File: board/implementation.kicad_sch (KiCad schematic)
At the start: 0 parts

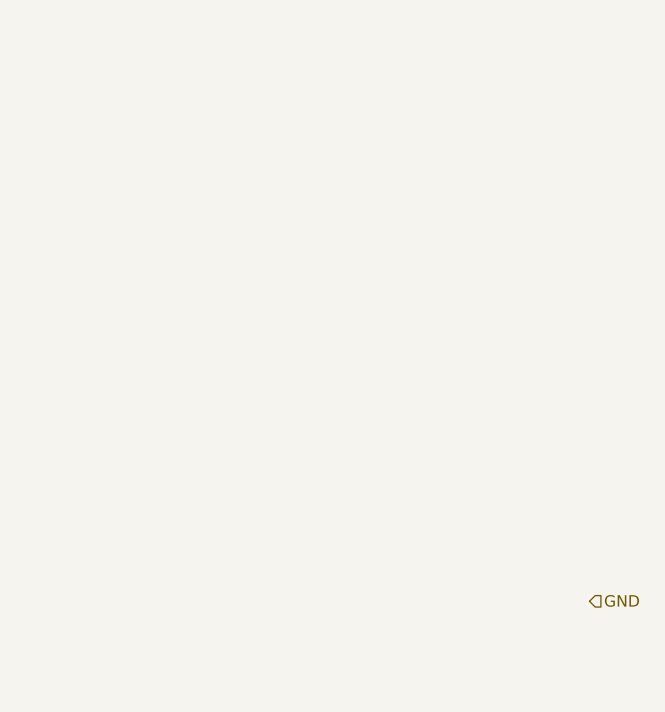
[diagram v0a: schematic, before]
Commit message: Add footprint, schema, 3D Model | Start circuit design
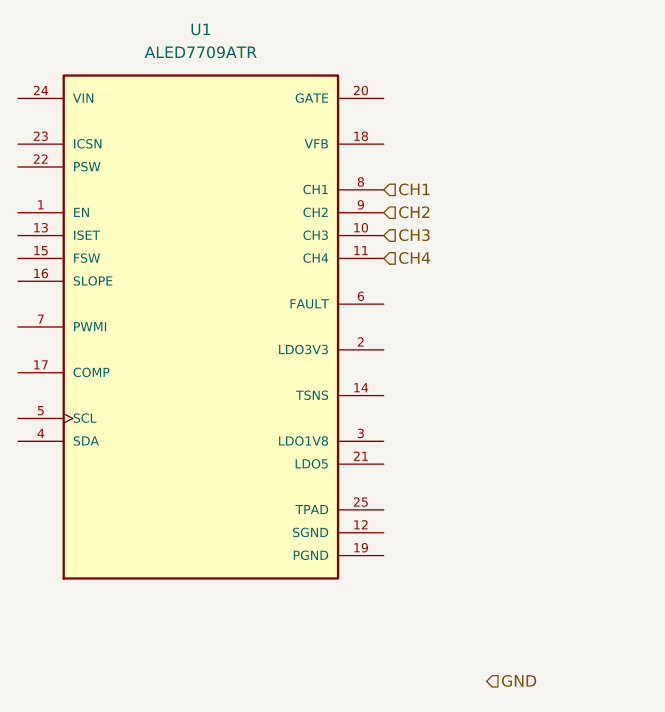
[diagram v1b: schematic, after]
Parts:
- added U1: ALED7709ATR, QFN65P500X500X90-25N, symbol ALED7709ATR:ALED7709ATR
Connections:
- new net CH1: U1.8 (CH1)
- new net CH2: U1.9 (CH2)
- new net CH3: U1.10 (CH3)
- new net CH4: U1.11 (CH4)
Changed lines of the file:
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@@
 (kicad_sch (version 20211123) (generator eeschema)
   (paper "A4")
-  (hierarchical_label "GND" (shape input) (at 194.31 120.65 0)
+  (hierarchical_label "CH1" (shape input) (at 171.45 74.93 0)
     (effects (font (size 1.27 1.27)) (justify left))
   )
+  (hierarchical_label "CH4" (shape input) (at 171.45 82.55 0)
+    (effects (font (size 1.27 1.27)) (justify left))
+  )
+  (hierarchical_label "GND" (shape input) (at 182.88 129.54 0)
+    (effects (font (size 1.27 1.27)) (justify left))
+  )
+  (hierarchical_label "CH3" (shape input) (at 171.45 80.01 0)
+    (effects (font (size 1.27 1.27)) (justify left))
+  )
+  (hierarchical_label "CH2" (shape input) (at 171.45 77.47 0)
+    (effects (font (size 1.27 1.27)) (justify left))
+  )
+  (symbol (lib_id "ALED7709ATR:ALED7709ATR") (at 151.13 90.17 0) (unit 1)
+    (in_bom yes) (on_board yes) (fields_autoplaced)
+    (property "Reference" "U1" (id 0) (at 151.13 57.15 0))
+    (property "Value" "ALED7709ATR" (id 1) (at 151.13 59.69 0))
+    (property "Footprint" "QFN65P500X500X90-25N" (id 2) (at 151.13 90.17 0)
+      (effects (font (size 1.27 1.27)) (justify bottom) hide)
+    )
+    (property "Datasheet" "https://www.st.com/resource/en/datasheet/aled7709.pdf" (id 3) (at 151.13 90.17 0)
+      (effects (font (size 1.27 1.27)) hide)
+    )
+    (property "SNAPEDA_PACKAGE_ID" "" (id 4) (at 151.13 90.17 0)
+      (effects (font (size 1.27 1.27)) (justify bottom) hide)
+    )
+    (property "B_NOM" "0.3" (id 5) (at 151.13 90.17 0)
+      (effects (font (size 1.27 1.27)) (justify bottom) hide)
+    )
+    (property "EMAX" "" (id 6) (at 151.13 90.17 0)
+      (effects (font (size 1.27 1.27)) (justify bottom) hide)
+    )
+    (property "D_MAX" "5.1" (id 7) (at 151.13 90.17 0)
+      (effects (font (size 1.27 1.27)) (justify bottom) hide)
+    )
+    (property "BALL_COLUMNS" "" (id 8) (at 151.13 90.17 0)
+      (effects (font (size 1.27 1.27)) (justify bottom) hide)
+    )
+    (property "PIN_COUNT_D" "6.0" (id 9) (at 151.13 90.17 0)
+      (effects (font (size 1.27 1.27)) (justify bottom) hide)
+    )
+    (property "THERMAL_PAD" "" (id 10) (at 151.13 90.17 0)
+      (effects (font (size 1.27 1.27)) (justify bottom) hide)
+    )
+    (property "DMAX" "" (id 11) (at 151.13 90.17 0)
+      (effects (font (size 1.27 1.27)) (justify bottom) hide)
+    )
+    (property "B_MAX" "0.35" (id 12) (at 151.13 90.17 0)
+      (effects (font (size 1.27 1.27)) (justify bottom) hide)
+    )
+    (property "EMIN" "" (id 13) (at 151.13 90.17 0)
+      (effects (font (size 1.27 1.27)) (justify bottom) hide)
+    )
+    (property "JEDEC" "" (id 14) (at 151.13 90.17 0)
+      (effects (font (size 1.27 1.27)) (justify bottom) hide)
+    )
+    (property "ENOM" "0.65" (id 15) (at 151.13 90.17 0)
+      (effects (font (size 1.27 1.27)) (justify bottom) hide)
+    )
+    (property "D_NOM" "5.0" (id 16) (at 151.13 90.17 0)
+      (effects (font (size 1.27 1.27)) (justify bottom) hide)
+    )
+    (property "VACANCIES" "" (id 17) (at 151.13 90.17 0)
+      (effects (font (size 1.27 1.27)) (justify bottom) hide)
+    )
+    (property "L_MAX" "0.5" (id 18) (at 151.13 90.17 0)
+      (effects (font (size 1.27 1.27)) (justify bottom) hide)
+    )
+    (property "A_MAX" "0.9" (id 19) (at 151.13 90.17 0)
+      (effects (font (size 1.27 1.27)) (justify bottom) hide)
+    )
+    (property "E2_NOM" "3.5" (id 20) (at 151.13 90.17 0)
+      (effects (font (size 1.27 1.27)) (justify bottom) hide)
+    )
+    (property "D2_NOM" "3.5" (id 21) (at 151.13 90.17 0)
+      (effects (font (size 1.27 1.27)) (justify bottom) hide)
+    )
+    (property "PARTREV" "1" (id 22) (at 151.13 90.17 0)
+      (effects (font (size 1.27 1.27)) (justify bottom) hide)
+    )
+    (property "DNOM" "" (id 23) (at 151.13 90.17 0)
+      (effects (font (size 1.27 1.27)) (justify bottom) hide)
+    )
+    (property "DMIN" "" (id 24) (at 151.13 90.17 0)
+      (effects (font (size 1.27 1.27)) (justify bottom) hide)
+    )
+    (property "E_NOM" "5.0" (id 25) (at 151.13 90.17 0)
+      (effects (font (size 1.27 1.27)) (justify bottom) hide)
+    )
+    (property "BALL_ROWS" "" (id 26) (at 151.13 90.17 0)
+      (effects (font (size 1.27 1.27)) (justify bottom) hide)
+    )
+    (property "B_MIN" "0.25" (id 27) (at 151.13 90.17 0)
+      (effects (font (size 1.27 1.27)) (justify bottom) hide)
+    )
+    (property "STANDARD" "IPC 7351B" (id 28) (at 151.13 90.17 0)
+      (effects (font (size 1.27 1.27)) (justify bottom) hide)
+    )
+    (property "L_NOM" "0.4" (id 29) (at 151.13 90.17 0)
+      (effects (font (size 1.27 1.27)) (justify bottom) hide)
+    )
+    (property "MANUFACTURER" "STMicroelectronics" (id 30) (at 151.13 90.17 0)
+      (effects (font (size 1.27 1.27)) (justify bottom) hide)
+    )
+    (property "IPC" "" (id 31) (at 151.13 90.17 0)
+      (effects (font (size 1.27 1.27)) (justify bottom) hide)
+    )
+    (property "PIN_COLUMNS" "" (id 32) (at 151.13 90.17 0)
+      (effects (font (size 1.27 1.27)) (justify bottom) hide)
+    )
+    (property "PIN_COUNT_E" "6.0" (id 33) (at 151.13 90.17 0)
+      (effects (font (size 1.27 1.27)) (justify bottom) hide)
+    )
+    (property "BODY_DIAMETER" "" (id 34) (at 151.13 90.17 0)
+      (effects (font (size 1.27 1.27)) (justify bottom) hide)
+    )
+    (property "E_MIN" "4.9" (id 35) (at 151.13 90.17 0)
+      (effects (font (size 1.27 1.27)) (justify bottom) hide)
+    )
+    (property "PACKAGE_TYPE" "" (id 36) (at 151.13 90.17 0)
+      (effects (font (size 1.27 1.27)) (justify bottom) hide)
+    )
+    (property "D_MIN" "4.9" (id 37) (at 151.13 90.17 0)
+      (effects (font (size 1.27 1.27)) (justify bottom) hide)
+    )
+    (property "PINS" "" (id 38) (at 151.13 90.17 0)
+      (effects (font (size 1.27 1.27)) (justify bottom) hide)
+    )
+    (property "L_MIN" "0.3" (id 39) (at 151.13 90.17 0)
+      (effects (font (size 1.27 1.27)) (justify bottom) hide)
+    )
+    (property "E_MAX" "5.1" (id 40) (at 151.13 90.17 0)
+      (effects (font (size 1.27 1.27)) (justify bottom) hide)
+    )
+    (pin "1")
+    (pin "10")
+    (pin "11")
+    (pin "12")
+    (pin "13")
+    (pin "14")
+    (pin "15")
+    (pin "16")
+    (pin "17")
+    (pin "18")
+    (pin "19")
+    (pin "2")
+    (pin "20")
+    (pin "21")
+    (pin "22")
+    (pin "23")
+    (pin "24")
+    (pin "25")
+    (pin "3")
+    (pin "4")
+    (pin "5")
+    (pin "6")
+    (pin "7")
+    (pin "8")
+    (pin "9")
+  )
 )

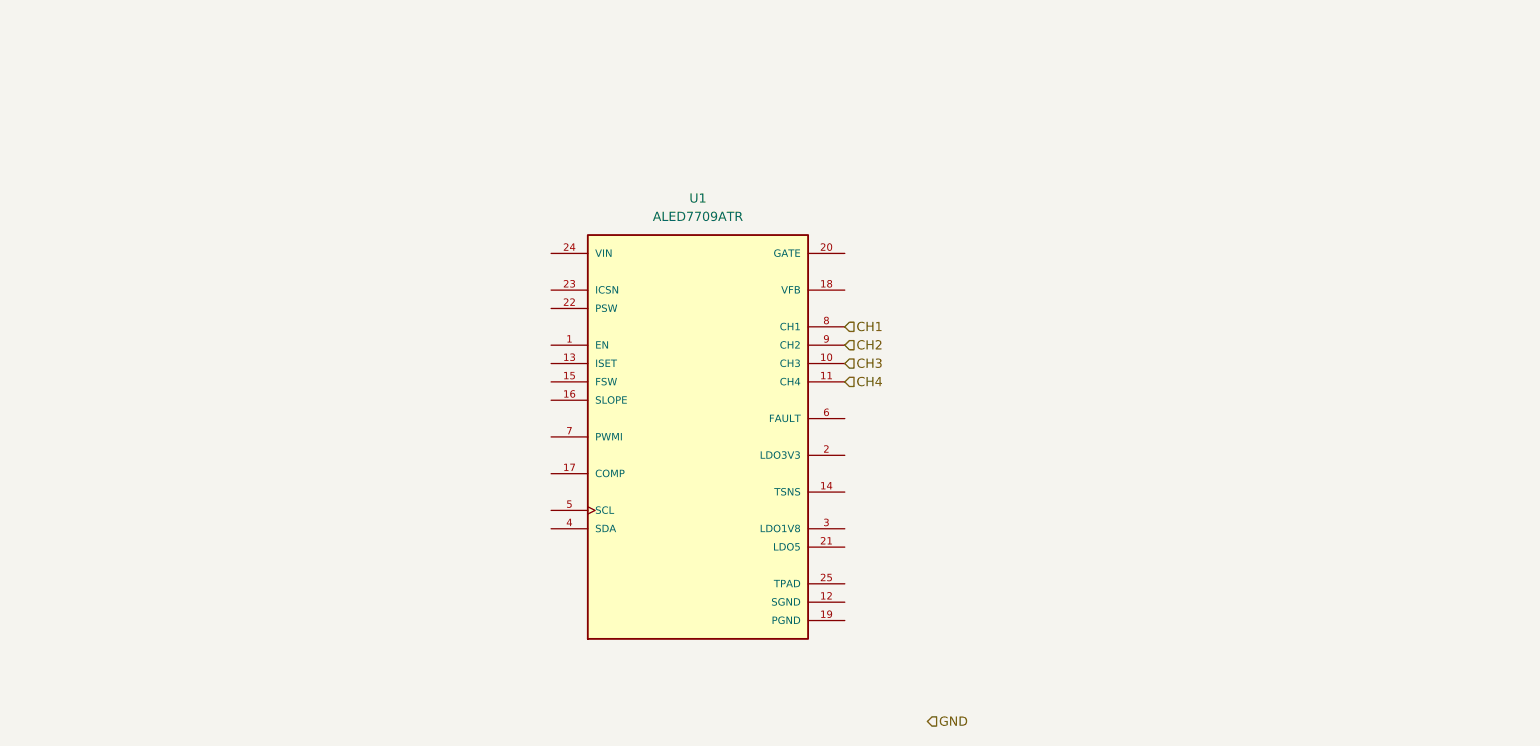
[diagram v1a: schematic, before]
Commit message: Add footprint, symbol and 3D modell | Add parts for reference cicuit
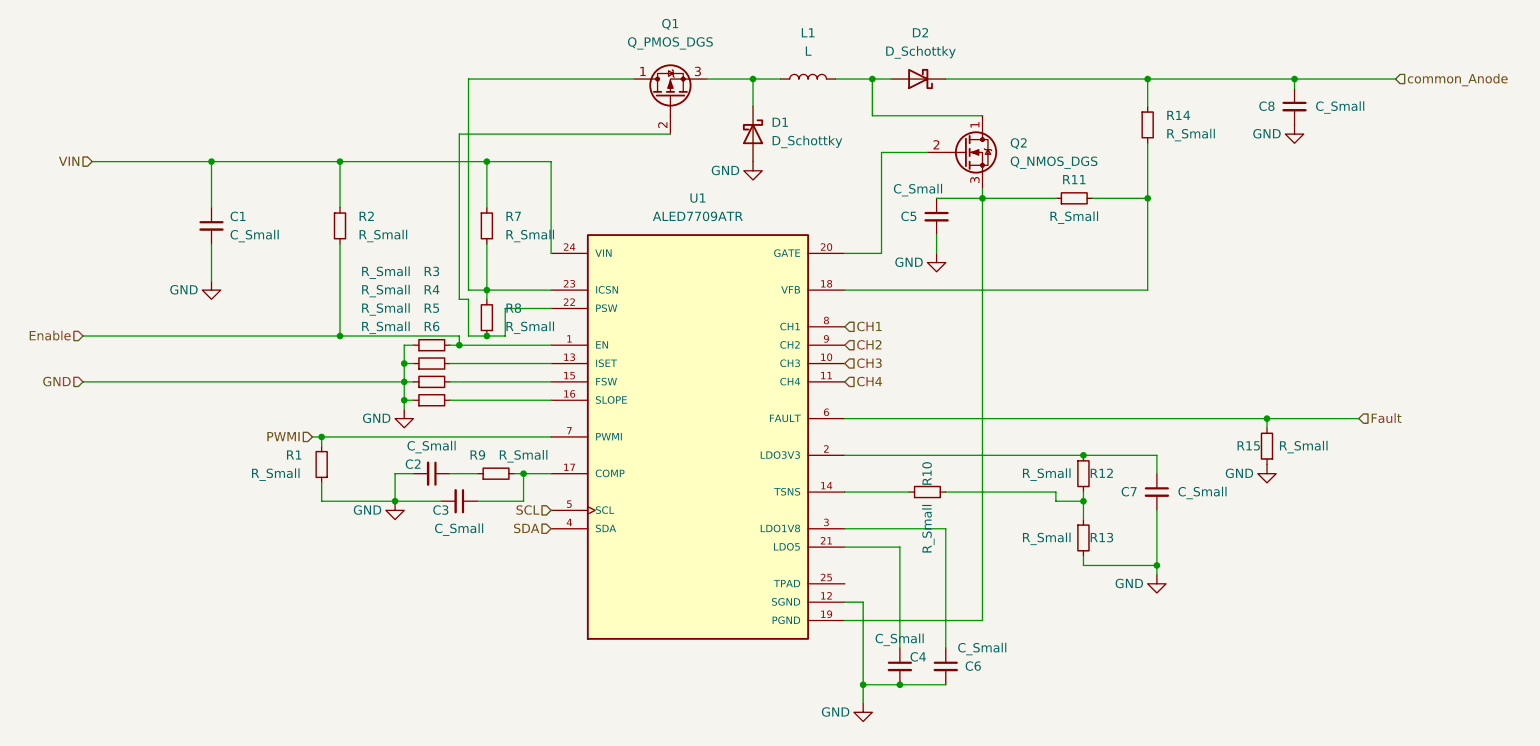
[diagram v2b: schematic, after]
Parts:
- added C1, C2, C3, C4, C5, C6, C7, C8: C_Small, Capacitor_SMD:C_0603_1608Metric, symbol Device:C_Small
- added D1: D_Schottky, Diode_SMD:D_SOD-123, symbol Device:D_Schottky
- added D2: D_Schottky, Diode_SMD:D_SMA, symbol Device:D_Schottky
- added L1: L, Inductor_SMD:L_12x12mm_H6mm, symbol Device:L
- added Q1: Q_PMOS_DGS, Package_TO_SOT_SMD:TO-252-3_TabPin2, symbol Device:Q_PMOS_DGS
- added Q2: Q_NMOS_DGS, led_treiber_edgy:TRANS_STL60P4LLF6, symbol Device:Q_NMOS_DGS
- added R1, R10, R11, R12, R13, R14, R15, R2, R3, R4, R5, R6, R7, R8, R9: R_Small, Resistor_SMD:R_0603_1608Metric, symbol Device:R_Small
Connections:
- net GND: now also U1.12 (SGND), C1.2, C2.2, C3.2, C4.2, C5.2, C6.2, C7.2, C8.2, D1.2 (A), R1.1, R13.2, R15.1, R3.1, R4.1, R5.1, R6.1
- net Enable: now reaches U1.1 (EN)
- net Enable: now also R2.2, R3.2
- net at U1.13 (ISET): now also R4.2
- net at U1.14 (TSNS): now also R10.1
- net at U1.15 (FSW): now also R5.2
- net at U1.16 (SLOPE): now also R6.2
- net at U1.17 (COMP): now also C3.1, R9.2
- net at U1.18 (VFB): now also R11.2, R14.2
- net at U1.19 (PGND): now also C5.1, Q2.3 (S), R11.1
- net at U1.2 (LDO3V3): now also C7.1, R12.1
- net at U1.20 (GATE): now also Q2.2 (G)
- net at U1.21 (LDO5): now also C4.1
- net at U1.22 (PSW): now also Q1.2 (G), R8.1
- net at U1.23 (ICSN): now also Q1.1 (D), R7.2, R8.2
- net VIN: now reaches U1.24 (VIN)
- net VIN: now also C1.1, R2.1, R7.1
- net at U1.3 (LDO1V8): now also C6.1
- net SDA: now reaches U1.4 (SDA)
- net SCL: now reaches U1.5 (SCL)
- net Fault: now reaches U1.6 (FAULT)
- net Fault: now also R15.2
- net PWMI: now reaches U1.7 (PWMI)
- net PWMI: now also R1.2
- new net: D2.2 (A), L1.2, Q2.1 (D)
- new net: R10.2, R12.2, R13.1
- new net: C2.1, R9.1
- new net: D1.1 (K), L1.1, Q1.3 (S)
- new net common_Anode: C8.1, D2.1 (K), R14.1

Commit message: Add routing
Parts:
- C1, C2, C3, C4, C5, C6, C7, C8: footprint Capacitor_SMD:C_0603_1608Metric -> Capacitor_SMD:C_0402_1005Metric
- L1: footprint Inductor_SMD:L_12x12mm_H6mm -> led_treiber_edgy:IND_XGL1010-332MED
- R1, R10, R11, R12, R13, R14, R15, R2, R3, R4, R5, R6, R7, R8, R9: footprint Resistor_SMD:R_0603_1608Metric -> Resistor_SMD:R_0402_1005Metric

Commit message: Update PCB
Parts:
- added D_Q2, D_Q3, G_Q2, G_Q3, S_Q2, S_Q3: TestPoint, TestPoint:TestPoint_Pad_D1.0mm, symbol Connector:TestPoint
- added TH1: 10kΩ, Resistor_SMD:R_0603_1608Metric, symbol Device:Thermistor_NTC
- C1, C8: value C_Small -> 10uF
- C4, C6, C7: value C_Small -> 1uF
- L1: value L -> 15uH
- R10: value R_Small -> 2kΩ
- R12: value R_Small -> 1,8kΩ
- R13: value R_Small -> 1.1kΩ
- R4: value R_Small -> 6,8kΩ
- R5: value R_Small -> 62kΩ
- R7: value R_Small -> 39 mΩ
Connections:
- net GND: now also TH1.2
- net at C5.1, Q2.3 (S), R11.1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: now also S_Q2.1
- net at D2.2 (A), L1.2, Q2.1 (D): now also D_Q2.1
- net at Q2.2 (G), U1.20 (GATE): now also G_Q2.1
- net at Q1.2 (G), R8.1, U1.22 (PSW): now also G_Q3.1
- net at Q1.1 (D), R7.2, R8.2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: now also D_Q3.1
- net at R10.2, R12.2, R13.1: now also TH1.1
- net at D1.1 (K), L1.1, Q1.3 (S): now also S_Q3.1

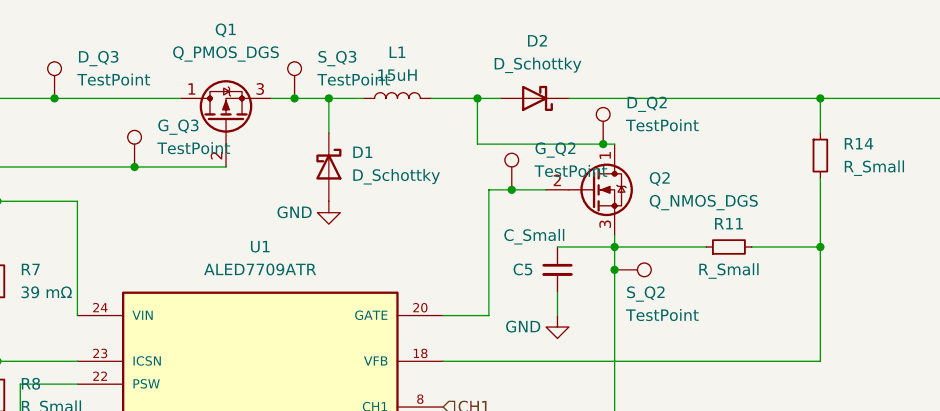
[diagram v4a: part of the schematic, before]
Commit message: Update footprint for MOSFETS
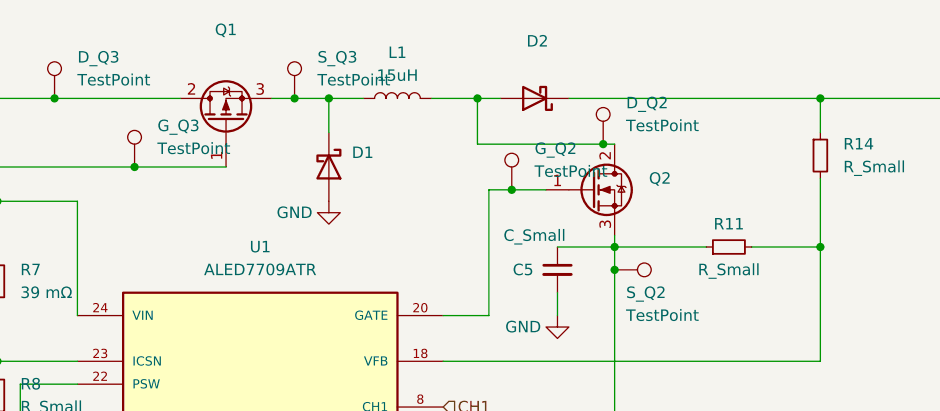
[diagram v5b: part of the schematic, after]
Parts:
- D1: value D_Schottky -> ~; MPN (none) -> STPS1H100
- D2: value D_Schottky -> ~; MPN (none) -> STPS2L60AY
- Q1: value Q_PMOS_DGS -> ~; footprint Package_TO_SOT_SMD:TO-252-3_TabPin2 -> Package_TO_SOT_SMD:TO-252-2; MPN (none) -> SQD50P08-25L_GE3
- Q2: value Q_NMOS_DGS -> ~; footprint led_treiber_edgy:TRANS_STL60P4LLF6 -> Package_TO_SOT_SMD:TO-252-2; MPN (none) -> MCU20N10-TP
- TH1: MPN (none) -> NCG18XH103F0SRB
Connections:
- net at D2.2 (A), D_Q2.1, L1.2: now also Q2.2 (D); no longer Q2.1 (D)
- net at G_Q2.1, U1.20 (GATE): now also Q2.1 (G); no longer Q2.2 (G)
- net at G_Q3.1, R8.1, U1.22 (PSW): now also Q1.1 (G); no longer Q1.2 (G)
- net at D_Q3.1, R7.2, R8.2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: now also Q1.2 (D); no longer Q1.1 (D)
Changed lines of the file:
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@@
+      (effects (font (size 1.27 1.27)) hide)
+    )
+    (property "MPN" "NCG18XH103F0SRB" (at 224.79 102.87 0)
       (effects (font (size 1.27 1.27)) hide)
     )
@@
       (effects (font (size 1.27 1.27)))
     )
-    (property "Value" "D_Schottky" (at 181.9275 36.83 0)
+    (property "Value" "~" (at 181.9275 36.83 0)
       (effects (font (size 1.27 1.27)))
     )
@@
       (effects (font (size 1.27 1.27)) hide)
     )
-    (property "Datasheet" "~" (at 181.61 40.64 0)
+    (property "Datasheet" "https://www.digikey.de/en/products/detail/stmicroelectronics/STPS2L60AY/2827020" (at 181.61 40.64 0)
+      (effects (font (size 1.27 1.27)) hide)
+    )
+    (property "MPN" "STPS2L60AY" (at 181.61 40.64 0)
       (effects (font (size 1.27 1.27)) hide)
     )
@@
       (effects (font (size 1.27 1.27)) (justify left))
     )
-    (property "Value" "Q_NMOS_DGS" (at 194.31 52.0699 0)
-      (effects (font (size 1.27 1.27)) (justify left))
-    )
-    (property "Footprint" "led_treiber_edgy:TRANS_STL60P4LLF6" (at 193.04 48.26 0)
-      (effects (font (size 1.27 1.27)) hide)
-    )
-    (property "Datasheet" "~" (at 187.96 50.8 0)
-      (effects (font (size 1.27 1.27)) hide)
-    )
-    (pin "1")
-    (pin "2")
+    (property "Value" "~" (at 194.31 52.0699 0)
+      (effects (font (size 1.27 1.27)) (justify left))
+    )
+    (property "Footprint" "Package_TO_SOT_SMD:TO-252-2" (at 193.04 48.26 0)
+      (effects (font (size 1.27 1.27)) hide)
+    )
+    (property "Datasheet" "https://www.digikey.de/en/products/detail/micro-commercial-co/MCU20N10-TP/14311630" (at 187.96 50.8 0)
+      (effects (font (size 1.27 1.27)) hide)
+    )
+    (property "MPN" "MCU20N10-TP" (at 187.96 50.8 0)
+      (effects (font (size 1.27 1.27)) hide)
+    )
+    (pin "2")
+    (pin "1")
     (pin "3")
     (instances
@@
       (effects (font (size 1.27 1.27)))
     )
-    (property "Value" "Q_PMOS_DGS" (at 147.32 35.56 90)
-      (effects (font (size 1.27 1.27)))
-    )
-    (property "Footprint" "Package_TO_SOT_SMD:TO-252-3_TabPin2" (at 144.78 38.1 0)
-      (effects (font (size 1.27 1.27)) hide)
-    )
-    (property "Datasheet" "~" (at 147.32 43.18 0)
-      (effects (font (size 1.27 1.27)) hide)
-    )
-    (pin "1")
-    (pin "2")
+    (property "Value" "~" (at 147.32 35.56 90)
+      (effects (font (size 1.27 1.27)))
+    )
+    (property "Footprint" "Package_TO_SOT_SMD:TO-252-2" (at 144.78 38.1 0)
+      (effects (font (size 1.27 1.27)) hide)
+    )
+    (property "Datasheet" "https://www.digikey.de/en/products/detail/vishay-siliconix/SQD50P08-25L-GE3/6595024" (at 147.32 43.18 0)
+      (effects (font (size 1.27 1.27)) hide)
+    )
+    (property "MPN" "SQD50P08-25L_GE3" (at 147.32 43.18 90)
+      (effects (font (size 1.27 1.27)) hide)
+    )
+    (pin "2")
+    (pin "1")
     (pin "3")
     (instances
@@
       (effects (font (size 1.27 1.27)) (justify left))
     )
-    (property "Value" "D_Schottky" (at 161.29 49.2124 90)
+    (property "Value" "~" (at 161.29 49.2124 90)
       (effects (font (size 1.27 1.27)) (justify left))
     )
@@
       (effects (font (size 1.27 1.27)) hide)
     )
-    (property "Datasheet" "~" (at 158.75 48.26 0)
-      (effects (font (size 1.27 1.27)) hide)
-    )
+    (property "Datasheet" "https://www.digikey.de/en/products/detail/stmicroelectronics/STPS1H100A/654555" (at 158.75 48.26 0)
+      (effects (font (size 1.27 1.27)) hide)
+    )
+    (property "MPN" "STPS1H100" (at 158.75 48.26 90)
+      (effects (font (size 1.27 1.27)) hide)
+    )
